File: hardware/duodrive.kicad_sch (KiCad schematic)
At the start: 92 parts, among them J1 Power, J2 Conn_01x04, J3 Conn_01x03, J4 MP2359, J6 Conn_01x04, J7 Conn_01x04, J8 Conn_01x04, Q1 AOD4184, Q2 AOD4184, Q3 AOD4184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

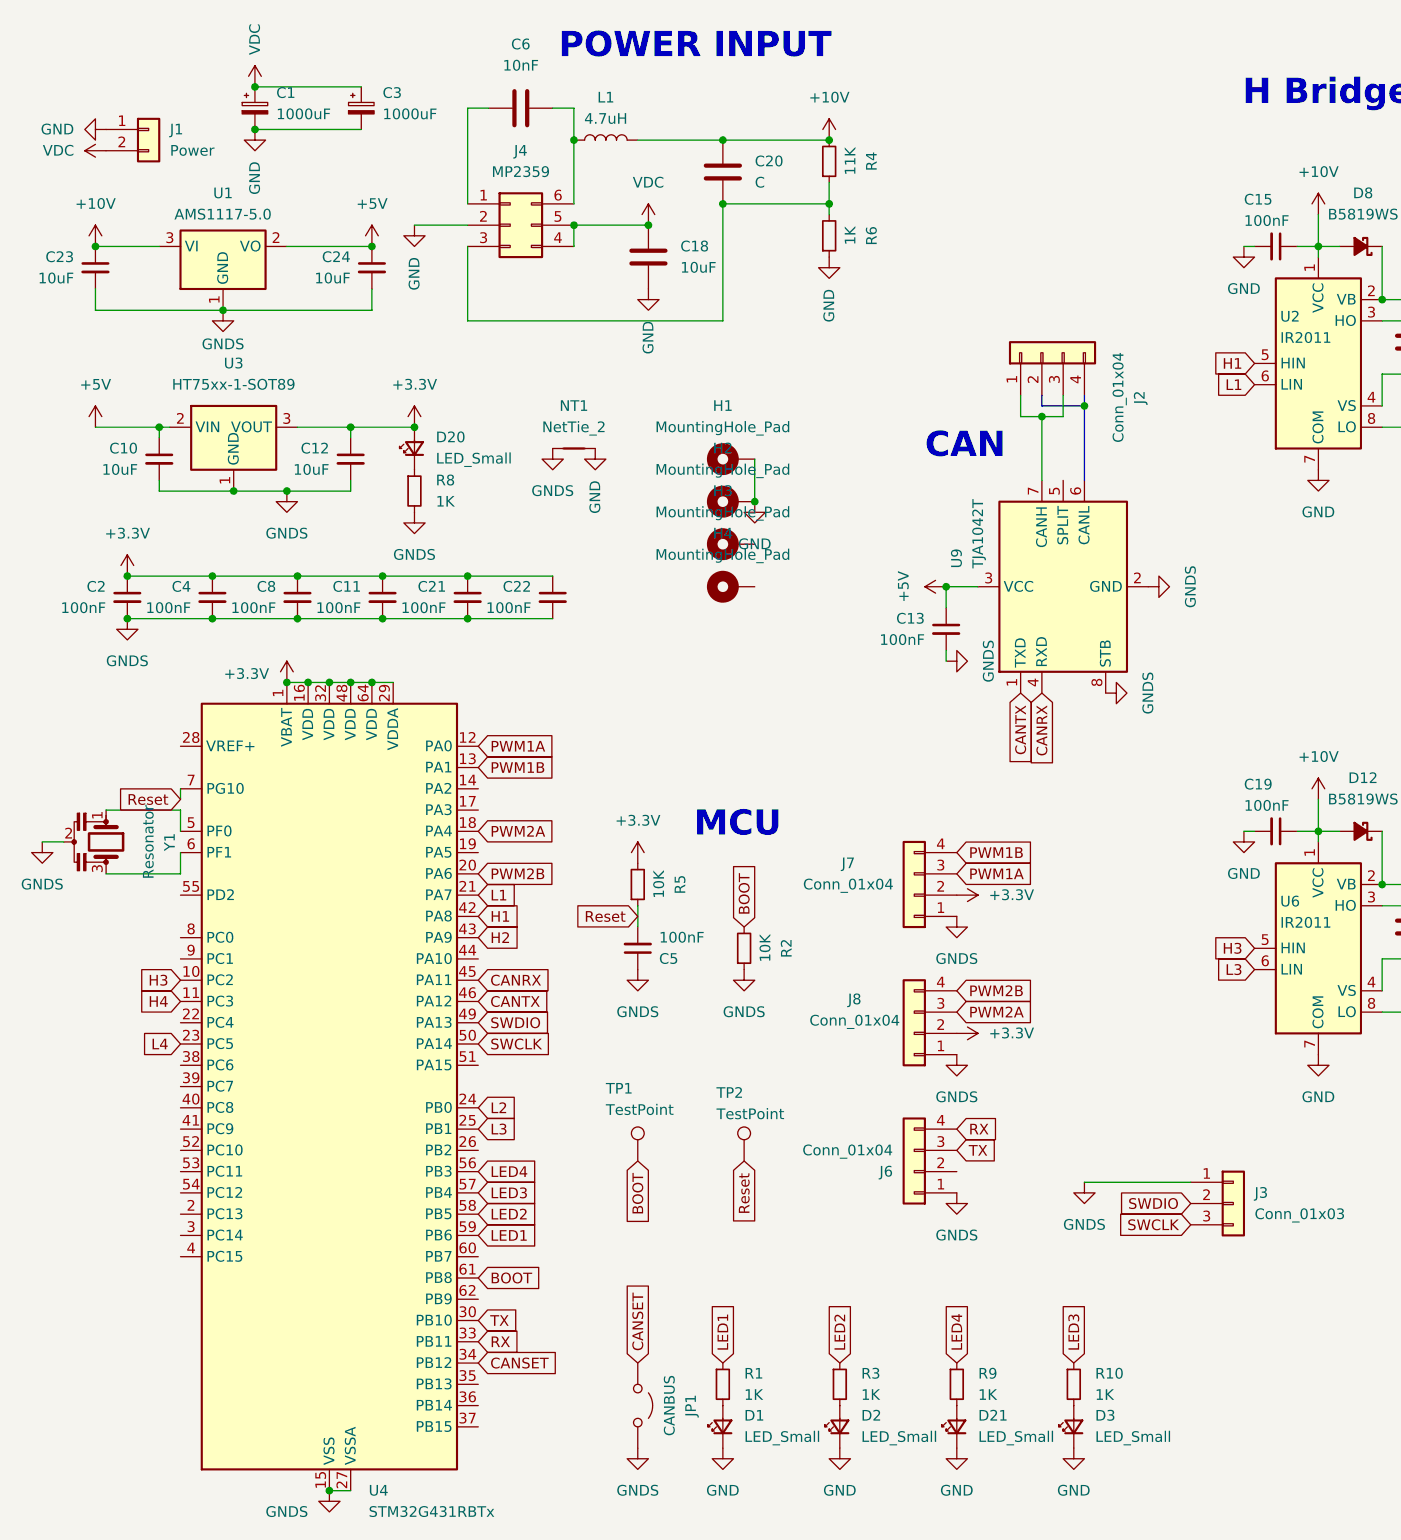
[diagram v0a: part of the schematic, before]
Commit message: Hardware bug fix
Fixed buck converter output bulk capacitor not connected to ground
Added pull up resistor at buck EN pin instead of connect it to VCC
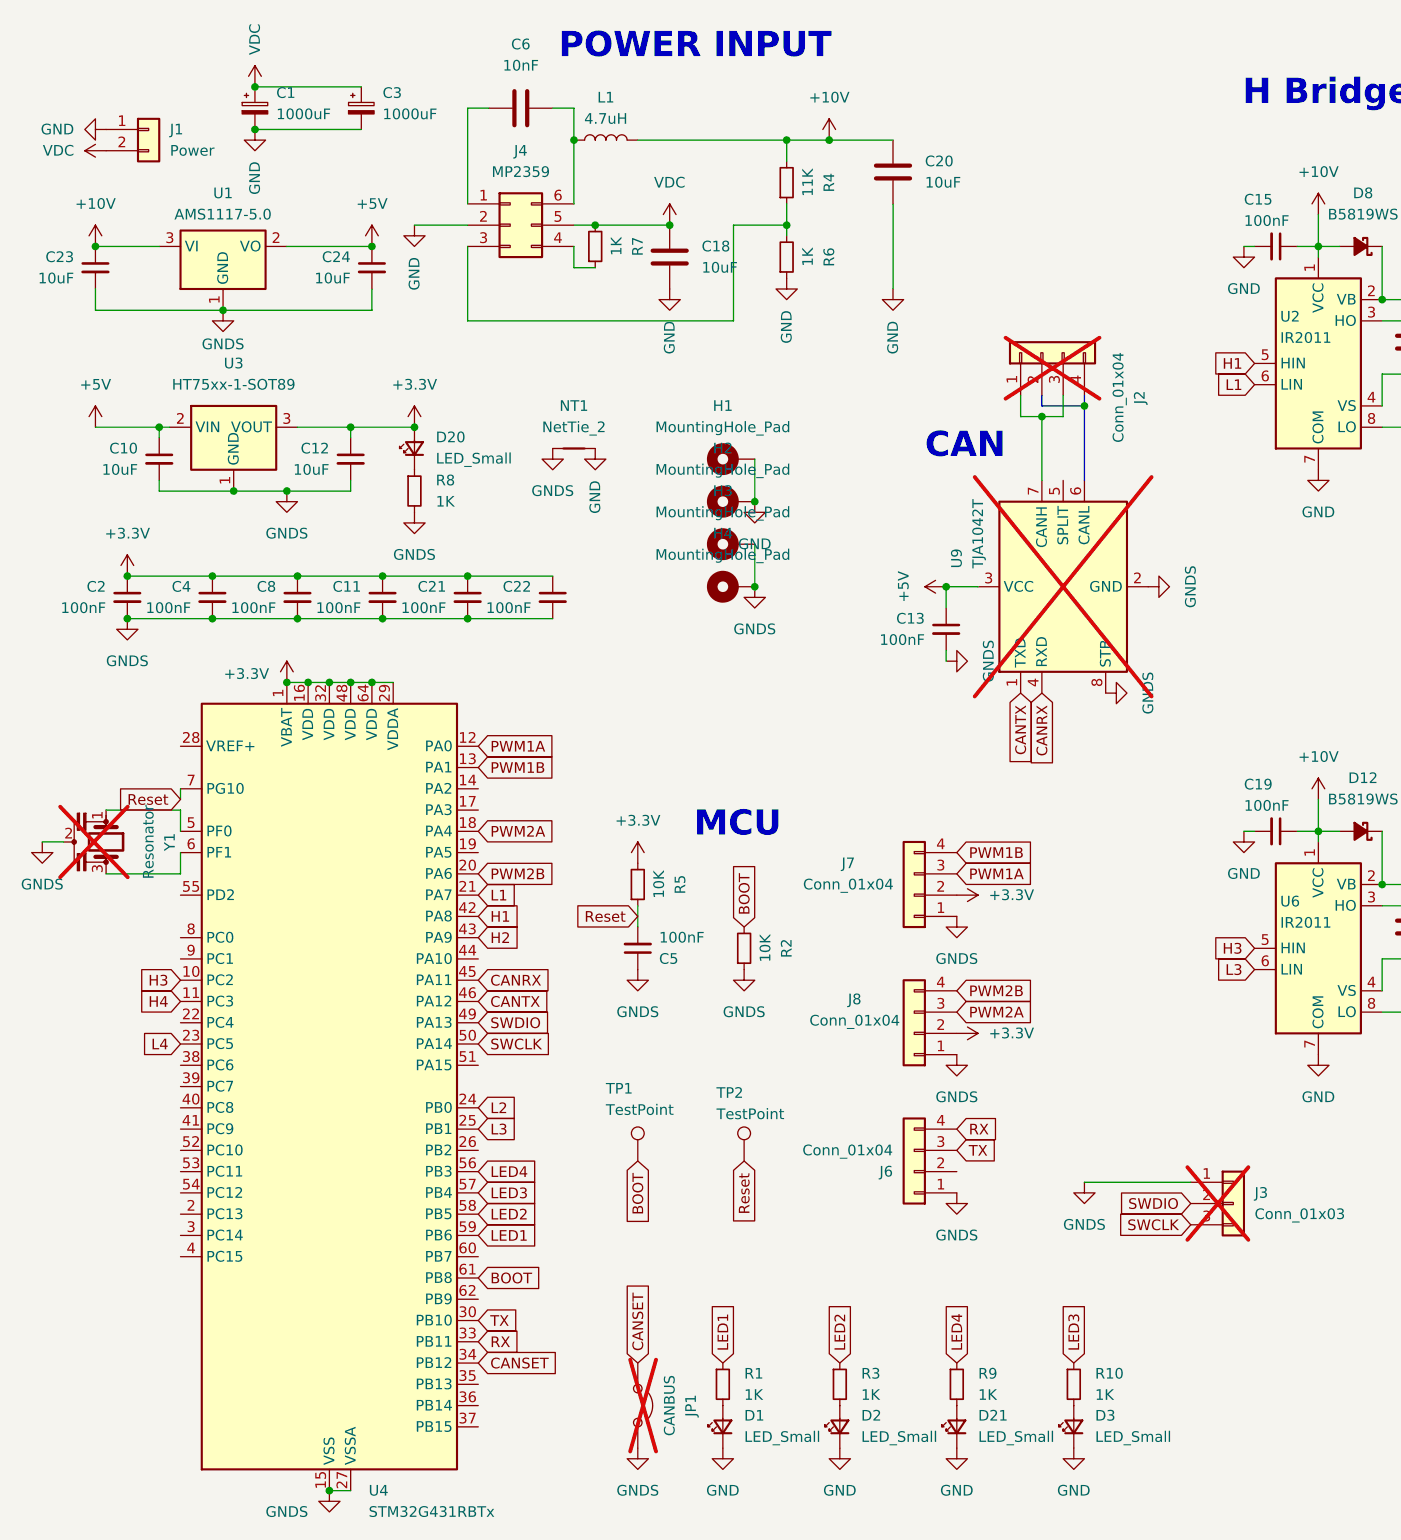
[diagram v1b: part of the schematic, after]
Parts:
- added R7: 1K, Resistor_SMD:R_0603_1608Metric, symbol Device:R_Small
- C20: value C -> 10uF; footprint Capacitor_SMD:C_1206_3216Metric -> Capacitor_SMD:C_1210_3225Metric
- H1, H2, H3, H4: footprint MountingHole:MountingHole_3.2mm_M3_DIN965_Pad -> MountingHole:MountingHole_3.2mm_M3
- J2, J3, JP1, U9, Y1: now not fitted
- TP1, TP2: now left out of the parts list
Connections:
- net GND: now also C20.1
- net GNDS: now also H3.1, H4.1
- net VDC: now also R7.2; no longer J4.4 (Pin_4)
- net at J4.3 (Pin_3), R4.1, R6.2: no longer C20.1
- new net: J4.4 (Pin_4), R7.1
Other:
- moved on the sheet: C18, C20, R4, R6

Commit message: Minor bug fix and QOL feature
Minor bug fix:
- Changed layout of buck converter for bigger capacitor and added pull up resistor
- Fixed buck output capacitor connected to wrong pin
- Changed passive component value to match final product value
QOL Feature:
- Added QR code on the bottom silkscreen for wiki page
- SWD connector changed from 2mm to 2.54mm for easier debug or update
- Grouping and separation in schematic layout for better visual clarity
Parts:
- C1, C3: value 1000uF -> 680uF
- C18, C20: value 10uF -> 22uF
- J3: footprint Connector_PinHeader_2.00mm:PinHeader_1x03_P2.00mm_Vertical -> Connector_PinHeader_2.54mm:PinHeader_1x03_P2.54mm_Vertical
- R4: value 11K -> 11.8K
- R7: value 1K -> 10K
- U1: footprint Package_TO_SOT_SMD:SOT-223-3_TabPin2 -> 1_NoOutline:SOT-223-3_TabPin2
- U2, U5, U6, U7, U9: footprint Package_SO:SOIC-8_3.9x4.9mm_P1.27mm -> 1_NoOutline:SOIC-8_3.9x4.9mm_P1.27mm
- U3: value HT75xx-1-SOT89 -> HT7833; footprint Package_TO_SOT_SMD:SOT-89-3 -> 1_NoOutline:SOT-89-3
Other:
- note added: "POWER"
- note removed: "POWER INPUT"
- moved on the sheet: C1, C10, C11, C12, C13, C14, C15, C16, C17, C18, C19, C2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

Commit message: NEW Version
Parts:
- removed J2: Conn_01x04, Connector_JST:JST_EH_S4B-EH_1x04_P2.50mm_Horizontal, symbol Connector_Generic:Conn_01x04
- removed J4: MP2359, Package_TO_SOT_SMD:SOT-23-6, symbol Connector_Generic:Conn_02x03_Counter_Clockwise
- removed J6: Conn_01x04, Connector_JST:JST_XH_B4B-XH-A_1x04_P2.50mm_Vertical, symbol Connector_Generic:Conn_01x04
- removed JP1: CANBUS, Connector_PinHeader_2.54mm:PinHeader_1x02_P2.54mm_Vertical, symbol Jumper:Jumper_2_Open
- removed U3: HT7833, 1_NoOutline:SOT-89-3, symbol Regulator_Linear:HT75xx-1-SOT89
- added C25: 33nF, Capacitor_SMD:C_0603_1608Metric, symbol Device:C
- added C26: 470pF, Capacitor_SMD:C_0603_1608Metric, symbol Device:C_Small
- added C27, C28: 22uF, Capacitor_SMD:C_1206_3216Metric, symbol Device:C
- added J10, J9: Power, TerminalBlock_Phoenix:TerminalBlock_Phoenix_PT-1,5-2-3.5-H_1x02_P3.50mm_Horizontal, symbol Connector_Generic:Conn_01x02
- added J12: Conn_02x09_Odd_Even, Connector_PinHeader_2.54mm:PinHeader_2x08_P2.54mm_Horizontal, symbol Connector_Generic:Conn_02x09_Odd_Even
- added JP2: Jumper_3_Open, Connector_PinHeader_2.54mm:PinHeader_1x03_P2.54mm_Vertical, symbol Jumper:Jumper_3_Open
- added R11: 1K, Resistor_SMD:R_0603_1608Metric, symbol Device:R_Small
- added R12: 10K, Resistor_SMD:R_0603_1608Metric, symbol Device:R_Small
- added U10: MIC5219-3.3YM5, Package_TO_SOT_SMD:SOT-23-5, symbol Regulator_Linear:MIC5219-3.3YM5
- added U8: TPS62933, Package_TO_SOT_SMD:SOT-583-8, symbol Regulator_Switching:TPS62933
- C18, C20: footprint Capacitor_SMD:C_1210_3225Metric -> Capacitor_SMD:C_1206_3216Metric
- C6: value 10nF -> 100nF
- D10, D11, D12, D13, D14, D15, D16, D17, D6, D7, D8, D9: footprint Diode_SMD:D_SOD-323 -> Diode_SMD:D_0805_2012Metric
- J3, U9: now fitted
- L1: value 4.7uH -> 12uH; footprint Inductor_SMD:L_Changjiang_FXL0420 -> Inductor_SMD:L_APV_ANR4020
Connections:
- net +10V: now also C28.2
- net +3.3V: now also JP2.3 (B), U10.5 (OUT); no longer J7.2 (Pin_2), J8.2 (Pin_2)
- net +5V: now also JP2.1 (A), U10.1 (IN), U10.3 (EN)
- net GND: now also C25.1, C27.1, C28.1, R11.1, R12.2, U8.4 (GND)
- net GNDS: now also C26.2, U10.2 (GND)
- net VDC: now also C27.2, U8.3 (VIN)
- net at R4.1, R6.2: now also U8.8 (FB)
- net at C14.2, Q7.3 (S), Q8.2 (D)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: now also J10.1 (Pin_1)
- net at R7.1: now also R12.1, U8.2 (EN)
- net at C9.2, Q3.3 (S), Q4.2 (D)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: now also J9.1 (Pin_1)
- net at C6.1: now also L1.1, U8.5 (SW)
- net at C6.2: now also U8.6 (BST); no longer L1.1
- net at C17.2, Q5.3 (S), Q6.2 (D)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: now also J10.2 (Pin_2)
- net at C7.2, Q1.3 (S), Q2.2 (D)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: now also J9.2 (Pin_2)
- new net: C26.1, U10.4 (BP)
- new net: R11.2, U8.1 (RT)
- new net: C25.2, U8.7 (SS)
- new net VBUS: J7.2 (Pin_2), J8.2 (Pin_2), JP2.2 (C)
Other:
- moved on the sheet: C10, C12, C18, C20, C23, C24, C5, C6, D20, H1, H2, H3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

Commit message: pcb
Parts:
- removed C23, C24: 10uF, Capacitor_SMD:C_0603_1608Metric, symbol Device:C_Small
- removed J12: Conn_02x09_Odd_Even, Connector_PinHeader_2.54mm:PinHeader_2x08_P2.54mm_Horizontal, symbol Connector_Generic:Conn_02x09_Odd_Even
- removed U1: AMS1117-5.0, 1_NoOutline:SOT-223-3_TabPin2, symbol Regulator_Linear:AMS1117-5.0
- added C29: 10uF, Capacitor_SMD:C_0805_2012Metric, symbol Device:C
- added C31: 22uF, Capacitor_SMD:C_0805_2012Metric, symbol Device:C
- added C41, C42: 100nF, Capacitor_SMD:C_0603_1608Metric, symbol Device:C
- added J2: Conn_02x08_Odd_Even, Connector_PinHeader_2.54mm:PinHeader_2x08_P2.54mm_Horizontal, symbol Connector_Generic:Conn_02x08_Odd_Even
- added L2: 2.2uH, Inductor_SMD_Wurth:L_Wurth_WE-LQSH-3012, symbol Device:L
- added U3: TPS62173DSG, Package_SON:WSON-8-1EP_2x2mm_P0.5mm_EP0.9x1.6mm_ThermalVias, symbol Regulator_Switching:TPS62172DSG
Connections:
- net +10V: now also C29.1, C41.1, U3.2 (VIN), U3.3 (EN)
- net +5V: now also C31.1, C42.1, L2.2, U3.6 (VOS)
- net GND: now also C29.2, C31.2, C41.2, C42.2, U3.1 (PGND), U3.4 (AGND), U3.5 (FB), U3.9 (PAD)
- new net: L2.1, U3.7 (SW)
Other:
- moved on the sheet: C18, C20, C25, C27, C28, C6, JP2, L1, R11, R12, R4, R6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

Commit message: test
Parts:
- added J4, J5: Conn_01x04, Connector_JST:JST_SH_SM04B-SRSS-TB_1x04-1MP_P1.00mm_Horizontal, symbol Connector_Generic:Conn_01x04
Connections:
- net +3.3V: now also J2.14 (Pin_14)
- net +5V: now also J2.8 (Pin_8)
- net GNDS: now also J2.1 (Pin_1), J2.7 (Pin_7), J4.1 (Pin_1), J5.1 (Pin_1)
- net H1: now also U4.8 (PC0); no longer U4.42 (PA8)
- net H2: now also U4.9 (PC1); no longer U4.43 (PA9)
- net RX: now also J2.15 (Pin_15)
- net TX: now also J2.16 (Pin_16)
- net PC6: now reaches J2.10 (Pin_10)
- net PC6: now also U4.38 (PC6)
- net SPI_MOSI: now reaches J2.11 (Pin_11)
- net SPI_MOSI: now also U4.37 (PB15)
- net SPI_MISO: now reaches J2.12 (Pin_12)
- net SPI_MISO: now also U4.36 (PB14)
- net SPI_CLK: now reaches J2.13 (Pin_13)
- net SPI_CLK: now also U4.35 (PB13)
- net PA9: now reaches J2.3 (Pin_3)
- net PA9: now also U4.43 (PA9)
- net PA8: now reaches J2.4 (Pin_4)
- net PA8: now also U4.42 (PA8)
- net PC9: now reaches J2.5 (Pin_5)
- net PC9: now also U4.41 (PC9)
- net PC8: now reaches J2.6 (Pin_6)
- net PC8: now also U4.40 (PC8)
- net PC7: now reaches J2.9 (Pin_9)
- net PC7: now also U4.39 (PC7)

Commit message: layout update
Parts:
- removed J1: Power, Connector_AMASS:AMASS_XT60-M_1x02_P7.20mm_Vertical, symbol Connector_Generic:Conn_01x02
- removed J10, J9: Power, TerminalBlock_Phoenix:TerminalBlock_Phoenix_PT-1,5-2-3.5-H_1x02_P3.50mm_Horizontal, symbol Connector_Generic:Conn_01x02
- added C23, C24: 1uF, Capacitor_SMD:C_0805_2012Metric, symbol Device:C
- added J6: Conn_01x06, TerminalBlock_MetzConnect:TerminalBlock_MetzConnect_Type094_RT03506HBLU_1x06_P5.00mm_Horizontal, symbol Connector_Generic:Conn_01x06
- C1, C3: footprint Capacitor_THT:CP_Radial_D10.0mm_P5.00mm -> Capacitor_SMD:C_Elec_10x10.2
- C15, C16, C19, C30: footprint Capacitor_SMD:C_0805_2012Metric -> Capacitor_SMD:C_0603_1608Metric
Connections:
- net GND: now also J6.3 (Pin_3)
- net VDC: now also J6.4 (Pin_4)
- net MOTOR_OUT_4: now reaches C14.2, Q7.3 (S), Q8.2 (D), U7.4 (VS)
- net MOTOR_OUT_4: now also J6.6 (Pin_6)
- net MOTOR_OUT_2: now reaches C9.2, Q3.3 (S), Q4.2 (D), U5.4 (VS)
- net MOTOR_OUT_2: now also J6.2 (Pin_2)
- net MOTOR_OUT_1: now reaches C7.2, Q1.3 (S), Q2.2 (D), U2.4 (VS)
- net MOTOR_OUT_1: now also J6.1 (Pin_1)
- net MOTOR_OUT_3: now reaches C17.2, Q5.3 (S), Q6.2 (D), U6.4 (VS)
- net MOTOR_OUT_3: now also J6.5 (Pin_5)

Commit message: update
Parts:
- added C32, C33, C34, C35: 1uF, Capacitor_SMD:C_0603_1608Metric, symbol Device:C
- C23, C24: value 1uF -> 22uF; footprint Capacitor_SMD:C_0805_2012Metric -> Capacitor_SMD:C_1206_3216Metric
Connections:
- net GND: now also C23.1, C24.1, C32.2, C33.2, C34.2, C35.2
- net VDC: now also C23.2, C24.2, C32.1, C33.1, C34.1, C35.1

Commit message: finish and polishing
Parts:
- removed U9: TJA1042T, 1_NoOutline:SOIC-8_3.9x4.9mm_P1.27mm, symbol Interface_CAN_LIN:TJA1042T
- added C36: 100nF, Capacitor_SMD:C_0603_1608Metric, symbol Device:C_Small
- added R21, R22: 47R, Resistor_SMD:R_0603_1608Metric, symbol Device:R_Small
- added U1: TCAN1044V, Package_SON:Texas_S-PVSON-N8_ThermalVias, symbol TiManh:TCAN1044V
- C1, C3: value 680uF -> 470uF
- J3: value Conn_01x03 -> SWD
- J4: value Conn_01x04 -> CAN_IN
- J5: value Conn_01x04 -> CAN_OUT
- J6: value Conn_01x06 -> POWER
- J7: value Conn_01x04 -> ENCODER1
- J8: value Conn_01x04 -> ENCODER2
- U2, U5, U6, U7: footprint 1_NoOutline:SOIC-8_3.9x4.9mm_P1.27mm -> Package_SO:SOIC-8_3.9x4.9mm_P1.27mm
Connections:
- net +3.3V: now also C36.1, U1.5 (VIO)
- net +5V: now also U1.3 (VCC)
- net CANRX: now also R21.1
- net CANTX: now also R22.1
- net CAN_H: now also J4.3 (Pin_3), J5.3 (Pin_3), U1.7 (CANH)
- net CAN_L: now also J4.2 (Pin_2), J5.2 (Pin_2), U1.6 (CANL)
- net GNDS: now also J2.2 (Pin_2), C36.2, U1.2 (GND), U1.8 (STB), U1.9 (THERMAL)
- new net: R22.2, U1.1 (TXD)
- new net: R21.2, U1.4 (RXD)
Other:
- moved on the sheet: C1, C10, C11, C12, C14, C15, C16, C17, C18, C19, C2, C20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
